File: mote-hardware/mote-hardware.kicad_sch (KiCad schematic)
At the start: 43 parts, among them J1 USB_B_Micro, J2 Conn_02x18_Odd_Even, J3 Conn_02x18_Odd_Even, J4 SM03B-SRSS-TB, SW1 SW_Push, SW2 SW_Push, U1 RP2350_60QFN, U2 NCP1117-3.3_SOT223, U3 W25Q128JVS, Y1 ABM8-272-T3

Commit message: First pass at RP2350 schematic
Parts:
- removed C1, C19, C5: 10u, Capacitor_SMD:C_0805_2012Metric, symbol Device:C
- removed C10, C9: 4.7u, Capacitor_SMD:C_0402_1005Metric, symbol Device:C
- removed C11, C12, C13, C14, C15, C16, C17, C18, C2, C8: 100n, Capacitor_SMD:C_0402_1005Metric, symbol Device:C
- removed C3, C4: 15p, Capacitor_SMD:C_0402_1005Metric, symbol Device:C
- removed C6, C7: 4.7u, RP2350_60QFN_minimal:C_0402_1005Metric_small_pads, symbol Device:C
- removed H1, H2, H3, H4: MountingHole, MountingHole:MountingHole_2.7mm_M2.5, symbol Mechanical:MountingHole
- removed J1: USB_B_Micro, Connector_USB:USB_Micro-B_Amphenol_10103594-0001LF_Horizontal, symbol Connector:USB_B_Micro
- removed J2, J3: Conn_02x18_Odd_Even, Connector_PinHeader_2.54mm:PinHeader_2x18_P2.54mm_Vertical, symbol Connector_Generic:Conn_02x18_Odd_Even
- removed J4: SM03B-SRSS-TB, Connector_JST:JST_SH_SM03B-SRSS-TB_1x03-1MP_P1.00mm_Horizontal, symbol Connector_Generic_MountingPin:Conn_01x03_MountingPin
- removed L1: 3.3u, RP2350_60QFN_minimal:L_pol_2016, symbol Device:L
- removed R1, R9: DNF, Resistor_SMD:R_0402_1005Metric, symbol Device:R
- removed R10: 0, Resistor_SMD:R_0402_1005Metric, symbol Device:R
- removed R2, R4, R6: 1k, Resistor_SMD:R_0402_1005Metric, symbol Device:R
- removed R5: 33, Resistor_SMD:R_0402_1005Metric, symbol Device:R
- removed R7, R8: 27, Resistor_SMD:R_0402_1005Metric, symbol Device:R
- removed SW1, SW2: SW_Push, Button_Switch_SMD:SW_Push_1P1T_NO_Vertical_Wuerth_434133025816, symbol Switch:SW_Push
- removed U1: RP2350_60QFN, RP2350_60QFN_minimal:RP2350-QFN-60-1EP_7x7_P0.4mm_EP3.4x3.4mm_ThermalVias, symbol MCU_RaspberryPi_RP2350:RP2350_60QFN
- removed U2: NCP1117-3.3_SOT223, Package_TO_SOT_SMD:SOT-223-3_TabPin2, symbol Regulator_Linear:NCP1117-3.3_SOT223
- removed U3: W25Q128JVS, Package_SO:SOIC-8_5.23x5.23mm_P1.27mm, symbol Memory_Flash:W25Q128JVS
- removed Y1: ABM8-272-T3, Crystal:Crystal_SMD_3225-4Pin_3.2x2.5mm, symbol Device:Crystal_GND24
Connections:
- no-connect marks 1 -> 0
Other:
- added sheet imu (imu.kicad_sch)
- added sheet lidar (rp_lidar_c1.kicad_sch)
- added sheet motors (motor.kicad_sch)
- added sheet power (power.kicad_sch)
- added sheet rp2354 (rp2354.kicad_sch)
- added sheet status leds (status_indicator.kicad_sch)
- note removed: "12MHz Crystal"
- note removed: "Flash"
- note removed: "IOs"
- note removed: "JST Debug Connector"
- note removed: "Make sure R7 and R8 are close to RP2350"
- note removed: "Power"

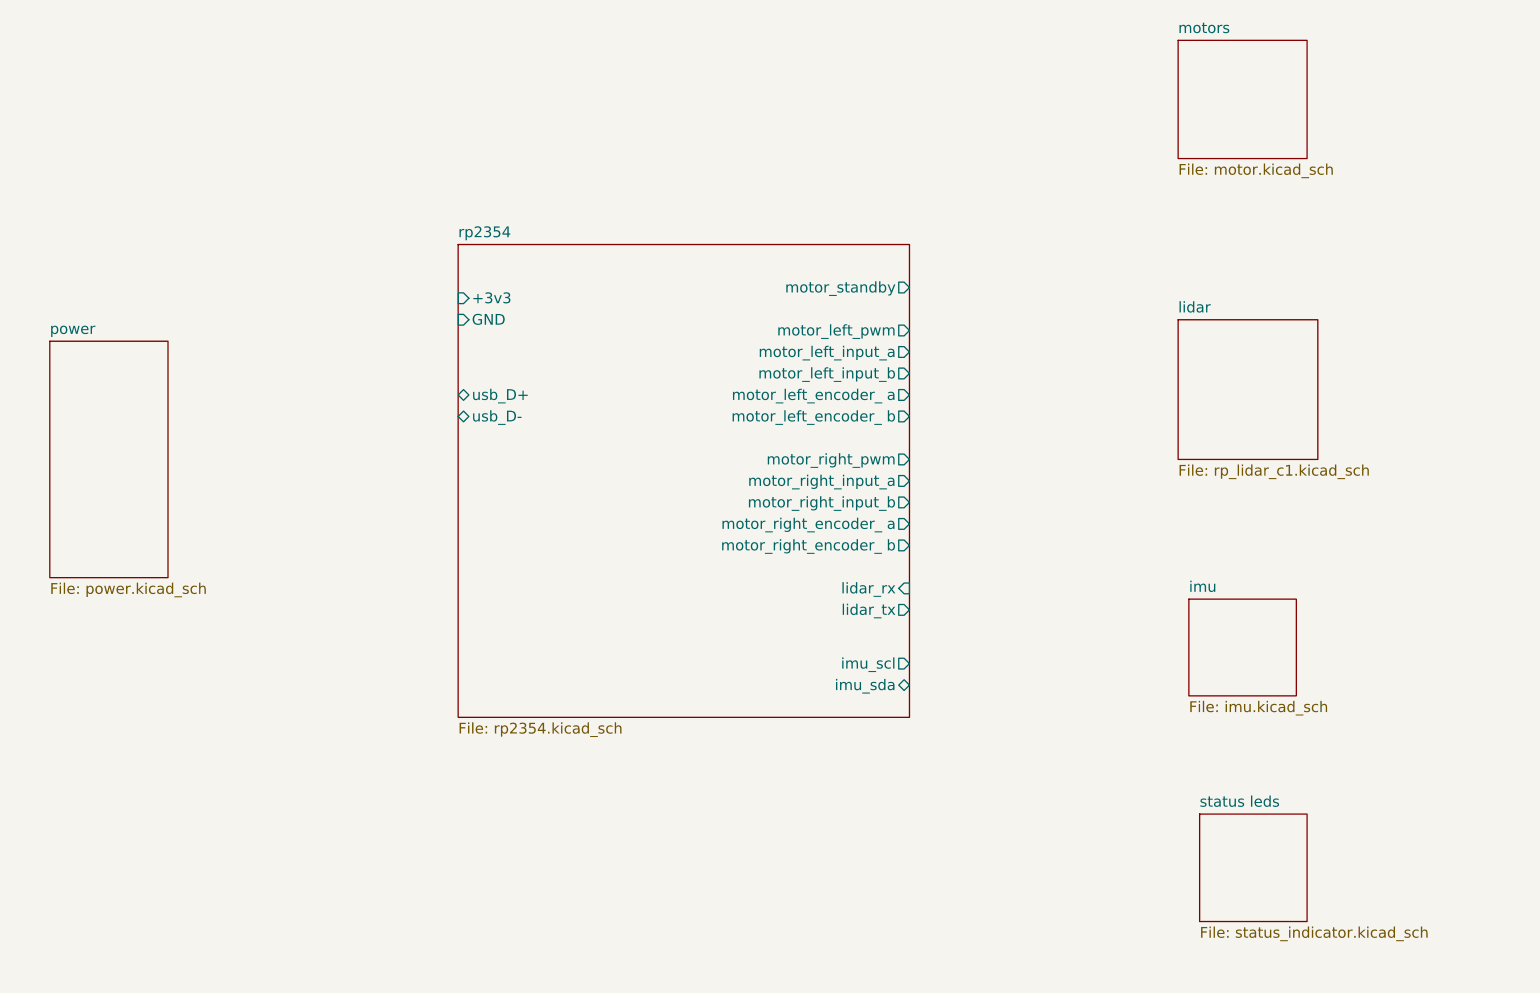
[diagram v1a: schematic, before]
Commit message: Implement motor, power, imu, status LED schematics
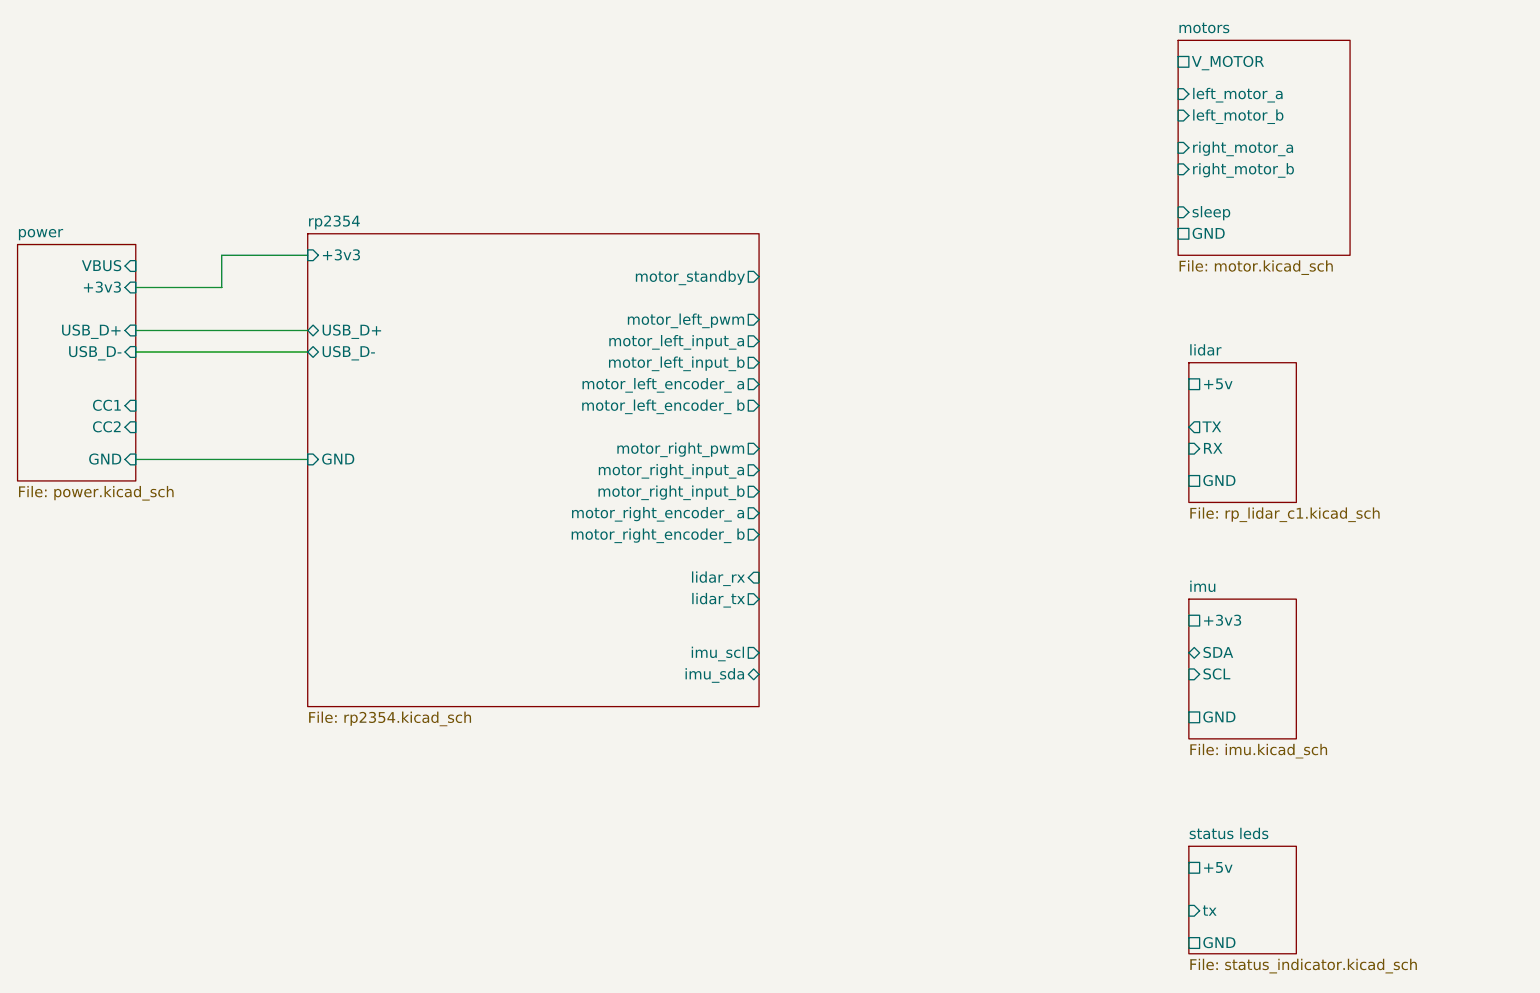
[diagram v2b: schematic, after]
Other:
- sheet imu ports: added +3v3, GND, SCL, SDA; removed none
- sheet lidar ports: added +5v, GND, RX, TX; removed none
- sheet motors ports: added GND, V_MOTOR, left_motor_a, left_motor_b, right_motor_a, right_motor_b, sleep; removed none
- sheet power ports: added +3v3, CC1, CC2, GND, USB_D+, USB_D-, VBUS; removed none
- sheet rp2354 ports: added USB_D+, USB_D-; removed usb_D+, usb_D-
- sheet status leds ports: added +5v, GND, tx; removed none

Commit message: First draft schematic complete
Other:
- sheet motors ports: added +3v3, left_encoder_a, left_encoder_b, right_encoder_a, right_encoder_b; removed none
- sheet rp2354 ports: added CC1, CC2, motor_left_encoder_a, motor_left_encoder_b, motor_right_encoder_a, motor_right_encoder_b, status_led_tx; removed motor_left_encoder_ a, motor_left_encoder_ b, motor_left_pwm, motor_right_encoder_ a, motor_right_encoder_ b, motor_right_pwm
- sheet status leds ports: added rx; removed tx
- note added: "Mote Top-Level Design"
- company: usedhondacivic -> github.com/usedhondacivic/mote
- title: Mote Circuit Board -> Mote

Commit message: Update date and github link
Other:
- company: github.com/usedhondacivic/mote -> github.com/empriselab/mote-core
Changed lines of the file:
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@@
 	(title_block
 		(title "Mote")
-		(date "2026-03-22")
+		(date "2026-03-31")
 		(rev "V0.0.0")
-		(company "github.com/usedhondacivic/mote")
+		(company "github.com/empriselab/mote-core")
 	)
 	(text "Mote Top-Level Design"

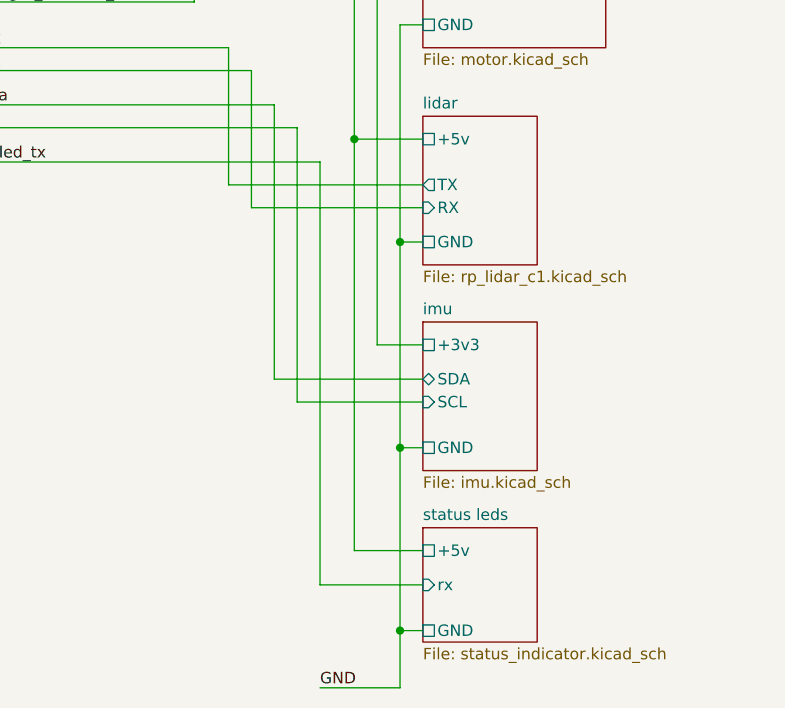
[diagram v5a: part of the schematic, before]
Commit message: 3v3 status LED not exposed at top level schematic
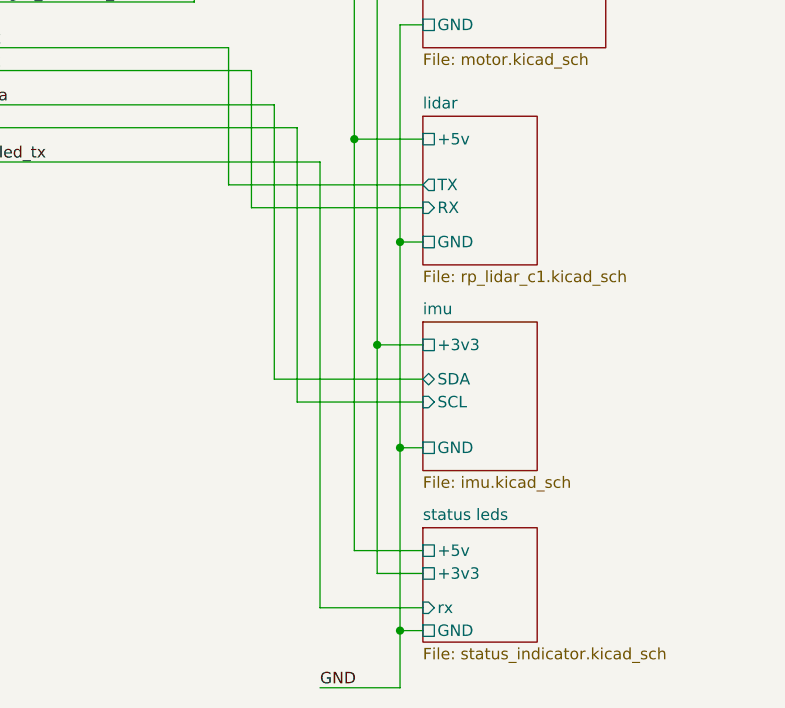
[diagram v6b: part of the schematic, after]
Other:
- sheet status leds ports: added +3v3; removed none
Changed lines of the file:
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@@
 	(title_block
 		(title "Mote")
-		(date "2026-03-31")
-		(rev "V0.0.0")
+		(date "2026-04-25")
+		(rev "V0.1.0")
 		(company "github.com/empriselab/mote-core")
 	)
@@
 	)
 	(junction
+		(at 200.66 119.38)
+		(diameter 0)
+		(color 0 0 0 0)
+	)
+	(junction
 		(at 198.12 96.52)
 		(diameter 0)
@@
 	(wire
 		(pts
+			(xy 205.74 144.78) (xy 200.66 144.78)
+		)
+		(stroke
+			(width 0)
+			(type default)
+		)
+	)
+	(wire
+		(pts
 			(xy 149.86 66.04) (xy 205.74 66.04)
 		)
@@
 	(wire
 		(pts
-			(xy 194.31 146.05) (xy 205.74 146.05)
+			(xy 194.31 148.59) (xy 205.74 148.59)
+		)
+		(stroke
+			(width 0)
+			(type default)
+		)
+	)
+	(wire
+		(pts
+			(xy 200.66 144.78) (xy 200.66 119.38)
 		)
 		(stroke
@@
 	(wire
 		(pts
-			(xy 194.31 99.06) (xy 194.31 146.05)
+			(xy 194.31 99.06) (xy 194.31 148.59)
 		)
 		(stroke
@@
 		)
 		(pin "rx" input
-			(at 205.74 146.05 180)
-			(effects
-				(font
+			(at 205.74 148.59 180)
+			(effects
+				(font
+					(size 1.27 1.27)
+				)
+				(justify left)
+			)
+		)
+		(pin "+3v3" passive
+			(at 205.74 144.78 180)
+			(effects
+				(font
